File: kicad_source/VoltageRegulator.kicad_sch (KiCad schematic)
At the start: 39 parts, among them P8 WR-TBL_691313710002, Q2 IPD90P03P4L- 04, U12 IFX91041EFJ, U13 INA226

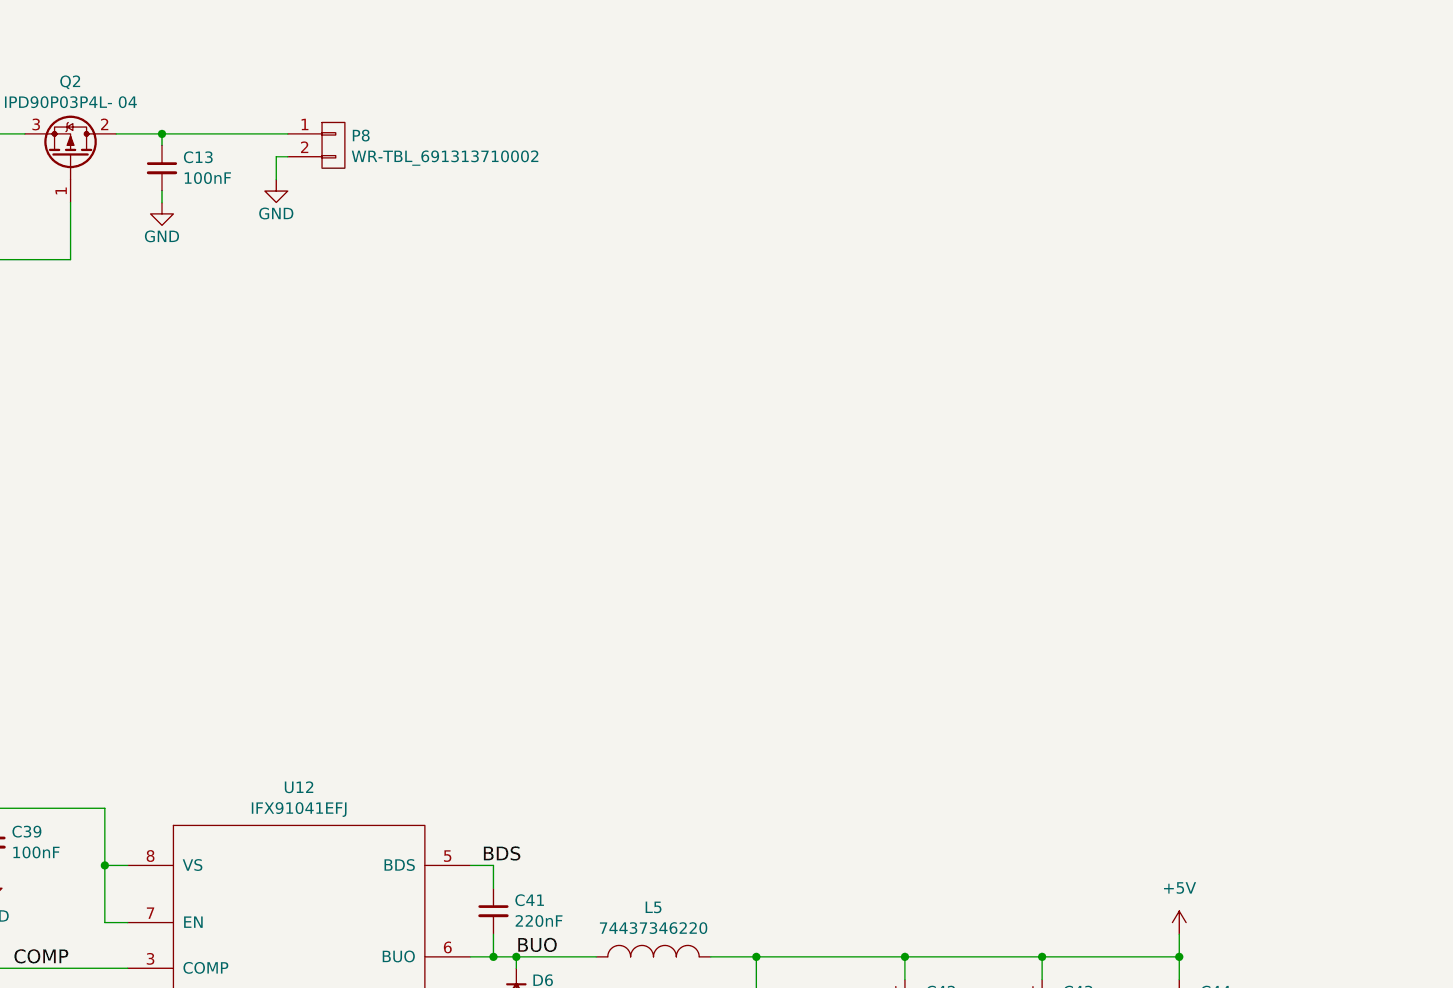
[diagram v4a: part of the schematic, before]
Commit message: added power pole and fuse
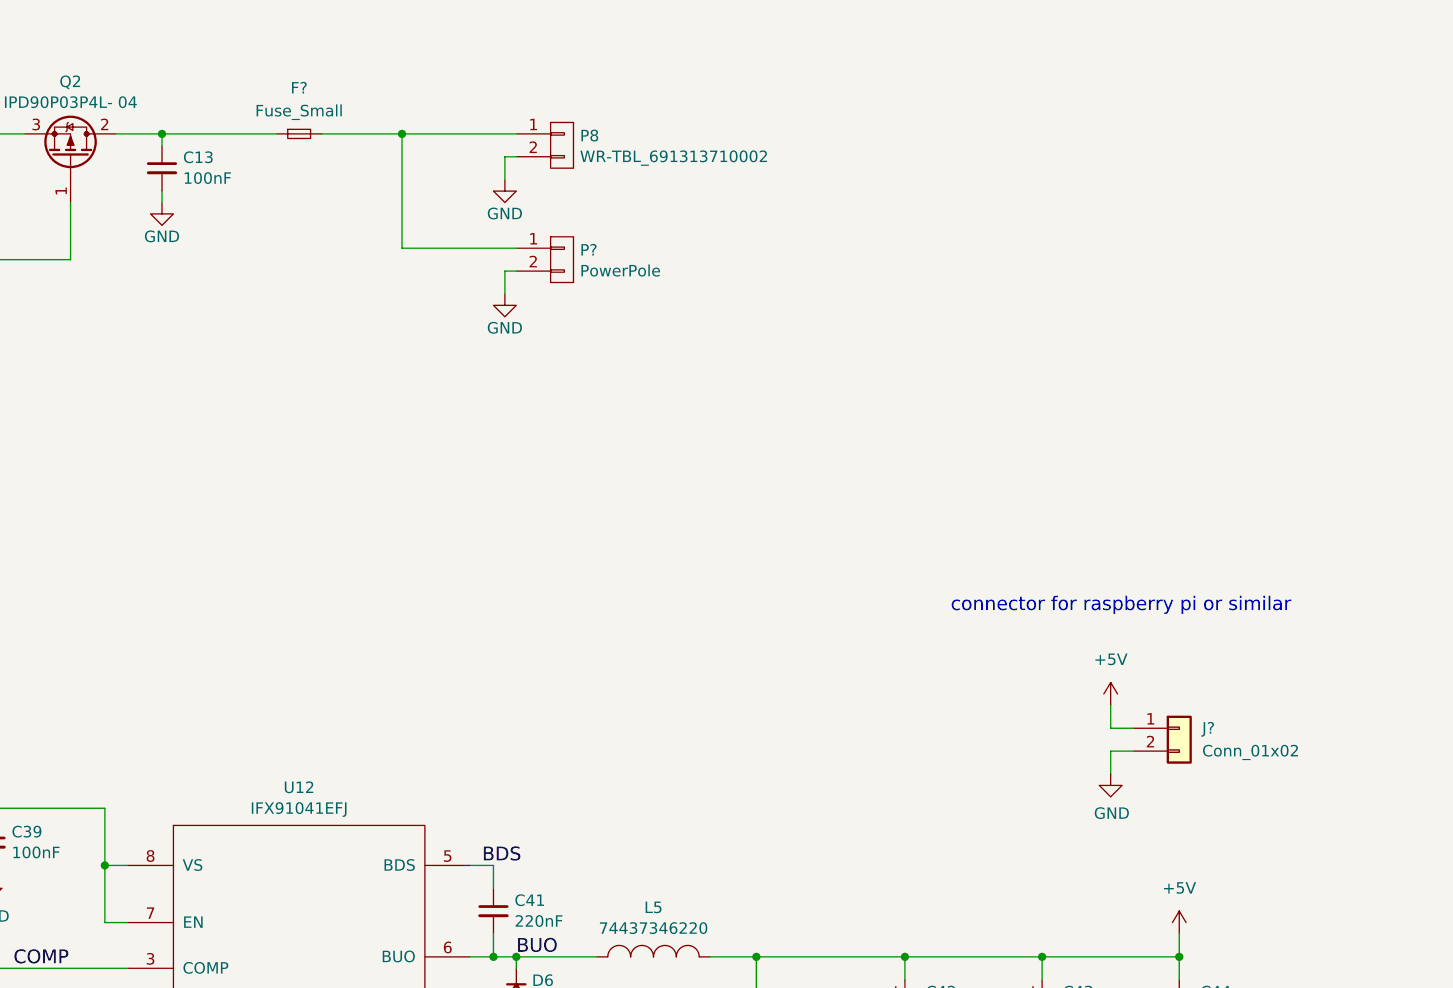
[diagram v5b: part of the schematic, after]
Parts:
- added F?: Fuse_Small, Fuse:Fuseholder_Blade_ATO_Littelfuse_Pudenz_2_Pin, symbol Device:Fuse_Small
- added J?: Conn_01x02, Connector_Phoenix_MC:PhoenixContact_MCV_1,5_2-G-3.81_1x02_P3.81mm_Vertical, symbol Connector_Generic:Conn_01x02
- added P?: PowerPole, generationmake:POWERPOLE_2, symbol OpenCyphalRobotController07-rescue:WR-TBL_691313710002-mechanical-connectors
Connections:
- net +5V: now also J?.1 (Pin_1)
- net GND: now also J?.2 (Pin_2), P?.2 (P2)
- net at C13.1, Q2.2 (D): now also F?.1; no longer P8.1 (P1)
- new net: F?.2, P8.1 (P1), P?.1 (P1)
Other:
- note added: "connector for raspberry pi or similar"
- moved on the sheet: P8

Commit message: started layout
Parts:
- gave numbers to parts that had none: 3
- renumbered C7 to C32, C9 to C33, C45 to C34, C11 to C35, C13 to C40, C40 to C41, C41 to C42, C42 to C43, C43 to C44, C44 to C45, D4 to D5, P8 to J10, R45 to R39, R46 to R40, R47 to R41, R11 to R42, R42 to R43, R43 to R44, R44 to R45, U13 to U12, U12 to U13

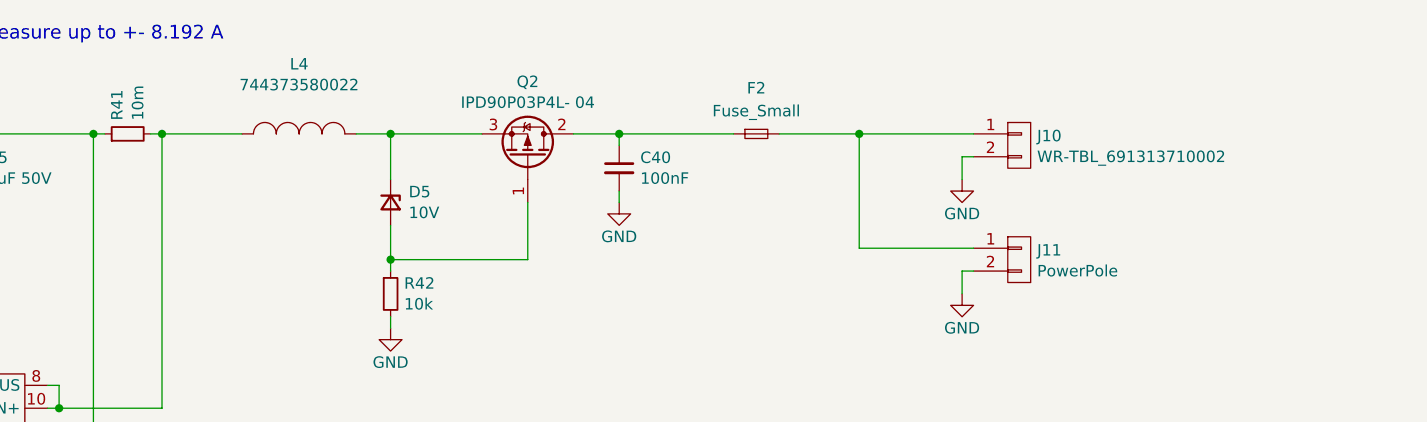
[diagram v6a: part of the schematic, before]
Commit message: made first draft of placement
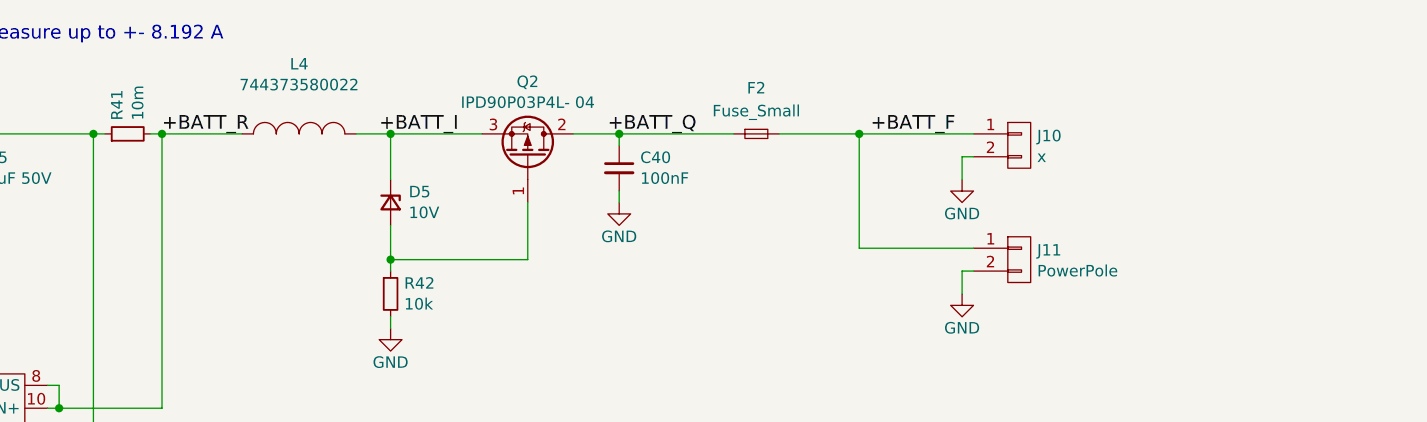
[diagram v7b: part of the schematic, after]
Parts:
- J10: value WR-TBL_691313710002 -> x; footprint CON_wuerth:WR-TBL_691313710002 -> Connector_Phoenix_MC:PhoenixContact_MCV_1,5_2-G-3.81_1x02_P3.81mm_Vertical
- Q2: footprint SOT_TO:TO-252-2Lead -> Package_TO_SOT_SMD:TO-252-2
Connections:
- net +BATT_F: now reaches F2.2, J10.1 (P1), J11.1 (P1)
- net +BATT_Q: now reaches C40.1, F2.1, Q2.2 (D)
- net +BATT_I: now reaches D5.1 (K), L4.2, Q2.3 (S)
- net +BATT_R: now reaches L4.1, R41.2, U12.10 (VIN+), U12.8 (VBUS)
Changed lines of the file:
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@@
+    (effects (font (size 1.524 1.524)) (justify left bottom))
+  )
+  (label "+BATT_I" (at 123.19 29.21 0)
+    (effects (font (size 1.524 1.524)) (justify left bottom))
+  )
+  (label "+BATT_R" (at 99.06 29.21 0)
     (effects (font (size 1.524 1.524)) (justify left bottom))
   )
@@
   )
   (label "BDS" (at 185.42 110.49 0)
+    (effects (font (size 1.524 1.524)) (justify left bottom))
+  )
+  (label "+BATT_F" (at 177.8 29.21 0)
+    (effects (font (size 1.524 1.524)) (justify left bottom))
+  )
+  (label "+BATT_Q" (at 148.59 29.21 0)
     (effects (font (size 1.524 1.524)) (justify left bottom))
   )
@@
       (effects (font (size 1.27 1.27)) (justify left))
     )
-    (property "Value" "WR-TBL_691313710002" (id 1) (at 196.2912 31.75 0)
-      (effects (font (size 1.27 1.27)) (justify left))
-    )
-    (property "Footprint" "CON_wuerth:WR-TBL_691313710002" (id 2) (at 191.77 29.21 0)
+    (property "Value" "x" (id 1) (at 196.2912 31.75 0)
+      (effects (font (size 1.27 1.27)) (justify left))
+    )
+    (property "Footprint" "Connector_Phoenix_MC:PhoenixContact_MCV_1,5_2-G-3.81_1x02_P3.81mm_Vertical" (id 2) (at 191.77 29.21 0)
       (effects (font (size 1.27 1.27)) hide)
     )
@@
     (property "Reference" "Q2" (id 0) (at 139.7 23.4188 90))
     (property "Value" "IPD90P03P4L- 04" (id 1) (at 139.7 25.7302 90))
-    (property "Footprint" "SOT_TO:TO-252-2Lead" (id 2) (at 142.24 26.67 0)
-      (effects (font (size 1.27 1.27)) hide)
-    )
+    (property "Footprint" "Package_TO_SOT_SMD:TO-252-2" (id 2) (at 142.24 26.67 0)
+      (effects (font (size 1.27 1.27)) hide)
+    )

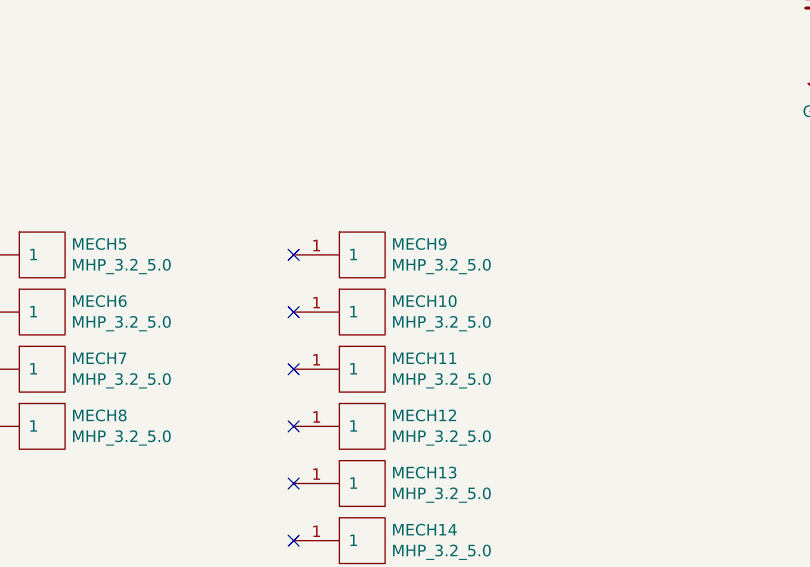
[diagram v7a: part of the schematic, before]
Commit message: updated layout
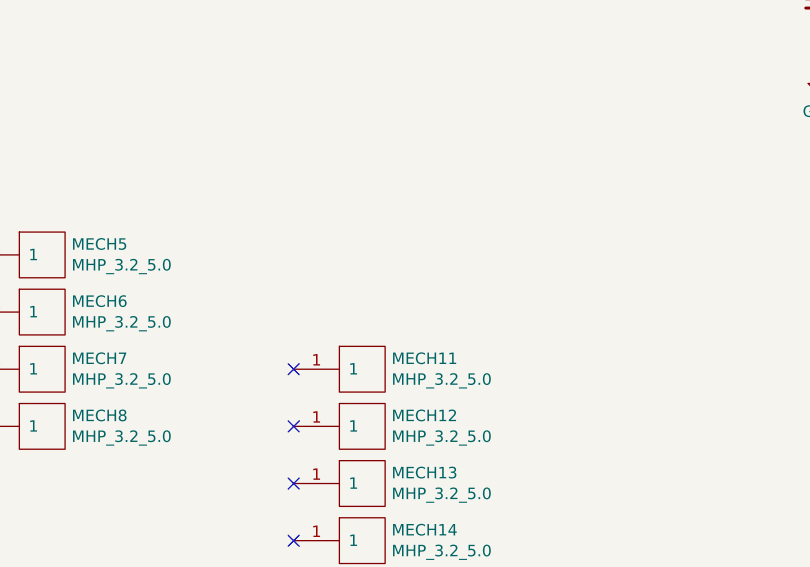
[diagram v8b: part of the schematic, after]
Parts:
- removed MECH10, MECH9: MHP_3.2_5.0, generationmake:MHP_3.2_5.8, symbol OpenCyphalRobotController07-rescue:MHP_3.2_5.0-MECH_mounting-holes
- L4: footprint L_power:WE-LHMI80xx -> Inductor_SMD:L_Wuerth_HCI-7050
- L5: footprint L_power:WE-LHMI70xx -> Inductor_SMD:L_Wuerth_HCI-7050
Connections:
- no-connect marks 11 -> 9
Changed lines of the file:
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@@
   )
   (no_connect (at 58.42 185.42))
-  (no_connect (at 58.42 160.02))
   (no_connect (at 22.86 166.37))
   (no_connect (at 22.86 160.02))
@@
   (no_connect (at 58.42 172.72))
   (no_connect (at 58.42 191.77))
-  (no_connect (at 58.42 166.37))
   (no_connect (at 58.42 179.07))
   (no_connect (at 22.86 172.72))
@@
     (property "Reference" "L5" (id 0) (at 204.47 115.189 0))
     (property "Value" "74437346220" (id 1) (at 204.47 117.5004 0))
-    (property "Footprint" "L_power:WE-LHMI70xx" (id 2) (at 204.47 117.5258 0)
+    (property "Footprint" "Inductor_SMD:L_Wuerth_HCI-7050" (id 2) (at 204.47 117.5258 0)
       (effects (font (size 1.27 1.27)) hide)
     )
@@
     )
     (property "Datasheet" "" (id 3) (at 30.48 179.07 0)
-      (effects (font (size 1.27 1.27)) hide)
-    )
-    (pin "1")
-  )
-  (symbol (lib_id "OpenCyphalRobotController07-rescue:MHP_3.2_5.0-MECH_mounting-holes") (at 66.04 160.02 0) (unit 1)
-    (in_bom yes) (on_board yes)
-    (property "Reference" "MECH9" (id 0) (at 69.2912 158.8516 0)
-      (effects (font (size 1.27 1.27)) (justify left))
-    )
-    (property "Value" "MHP_3.2_5.0" (id 1) (at 69.2912 161.163 0)
-      (effects (font (size 1.27 1.27)) (justify left))
-    )
-    (property "Footprint" "generationmake:MHP_3.2_5.8" (id 2) (at 63.5 158.75 0)
-      (effects (font (size 1.27 1.27)) hide)
-    )
-    (property "Datasheet" "" (id 3) (at 66.04 160.02 0)
-      (effects (font (size 1.27 1.27)) hide)
-    )
-    (pin "1")
-  )
-  (symbol (lib_id "OpenCyphalRobotController07-rescue:MHP_3.2_5.0-MECH_mounting-holes") (at 66.04 166.37 0) (unit 1)
-    (in_bom yes) (on_board yes)
-    (property "Reference" "MECH10" (id 0) (at 69.2912 165.2016 0)
-      (effects (font (size 1.27 1.27)) (justify left))
-    )
-    (property "Value" "MHP_3.2_5.0" (id 1) (at 69.2912 167.513 0)
-      (effects (font (size 1.27 1.27)) (justify left))
-    )
-    (property "Footprint" "generationmake:MHP_3.2_5.8" (id 2) (at 63.5 165.1 0)
-      (effects (font (size 1.27 1.27)) hide)
-    )
-    (property "Datasheet" "" (id 3) (at 66.04 166.37 0)
       (effects (font (size 1.27 1.27)) hide)
     )
@@
     (property "Reference" "L4" (id 0) (at 114.3 21.463 0))
     (property "Value" "744373580022" (id 1) (at 114.3 23.7744 0))
-    (property "Footprint" "L_power:WE-LHMI80xx" (id 2) (at 114.3 26.0858 0)
-      (effects (font (size 1.27 1.27)) hide)
-    )
+    (property "Footprint" "Inductor_SMD:L_Wuerth_HCI-7050" (id 2) (at 114.3 26.0858 0)
+      (effects (font (size 1.27 1.27)) hide)
+    )
